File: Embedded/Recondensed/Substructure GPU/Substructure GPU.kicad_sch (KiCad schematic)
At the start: 37 parts, among them J1 10171746-00021LF, J11 Substructure Power, J13 MicroSD, J2 HUB75 Right, J3 Display Power, J4 HUB75 Left, J5 Expansion Data, J6 Expansion PWR, SW2 RST, U2 74HC245D_653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

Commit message: Added LCSC Component IDs
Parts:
- removed BootSW1: SW_Push, Buttons:R-667843, symbol Switch:SW_Push
- removed SW2: RST, Buttons:R-667843, symbol Switch:SW_Push
- added S1: Boot, Buttons:SW_B3U-1000P, symbol Buttons:B3U-1000P
- added S2: RST, Buttons:SW_B3U-1000P, symbol Buttons:B3U-1000P
- C1, C10, C12, C2: LCSC (none) -> C1591
- C11, C8: LCSC (none) -> C84419
- C3, C4, C5: LCSC (none) -> C3039698
- C6: LCSC (none) -> C95843
- C7, C9: LCSC C95839 -> C3039698
- D1, D2: LCSC (none) -> C7207730
- D3: LCSC (none) -> C50603
- J1: footprint USBC:AMPHENOL_10171746-00021LF -> USBC:MOLEX_2171790001; LCSC (none) -> C3197684
- J13: LCSC (none) -> C587826
- J2, J4: LCSC C30734 -> C492425
- R1, R2: LCSC (none) -> C328432
- R4, R9: LCSC (none) -> C98220
- R7: value 155ohm min -> 147ohm; LCSC (none) -> C2930065
- R8: value 70ohm min -> 33ohm; LCSC (none) -> C105588
- U6: LCSC (none) -> C86781
- U7: LCSC (none) -> C134077
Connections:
- net GND: now also J1.A1B12 (GND_A), J1.B1A12 (GND_B), S1.2, S2.2; no longer J1.A1_B12 (GND_A), J1.B1_A12 (GND_B)
- net at C5.1, D3.A: now also J1.A4B9 (VBUS_A), J1.B4A9 (VBUS_B); no longer J1.A4_B9 (VBUS_A), J1.B4_A9 (VBUS_B)
- net at ESP1.27 (GPIO0/BOOT), R4.2: now also S1.1
- net at C6.2, ESP1.3 (EN), R9.2: now also S2.1

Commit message: Modified Tables per component to centralise LCSC IDs
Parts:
- ESP1, J11, J3, J5, J6, U5: now left out of the parts list
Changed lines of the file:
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@@
 		(unit 1)
 		(exclude_from_sim no)
-		(in_bom yes)
+		(in_bom no)
 		(on_board yes)
 		(dnp no)
@@
 			)
 		)
-		(property "PARTREV" "A"
+		(property "LCSC" "C3197684"
 			(at 31.75 38.1 0)
 			(effects
@@
 					(size 1.27 1.27)
 				)
-				(justify bottom)
 				(hide yes)
 			)
 		)
-		(property "STANDARD" "Manufacturer Recommendations"
+		(property "PARTREV" "A"
 			(at 31.75 38.1 0)
 			(effects
@@
 			)
 		)
-		(property "MAXIMUM_PACKAGE_HEIGHT" "3.16 mm"
+		(property "STANDARD" "Manufacturer Recommendations"
 			(at 31.75 38.1 0)
 			(effects
@@
 			)
 		)
-		(property "MANUFACTURER" "Amphenol"
+		(property "MAXIMUM_PACKAGE_HEIGHT" "3.16 mm"
 			(at 31.75 38.1 0)
 			(effects
@@
 			)
 		)
-		(property "LCSC" "C3197684"
+		(property "MANUFACTURER" "Amphenol"
 			(at 31.75 38.1 0)
 			(effects
@@
 					(size 1.27 1.27)
 				)
+				(justify bottom)
 				(hide yes)
 			)
@@
 		(unit 1)
 		(exclude_from_sim no)
-		(in_bom yes)
+		(in_bom no)
 		(on_board yes)
 		(dnp no)
@@
 			)
 		)
+		(property "LCSC" "C5625"
+			(at 280.67 213.36 0)
+			(effects
+				(font
+					(size 1.27 1.27)
+				)
+				(hide yes)
+			)
+		)
 		(property "MF" "Nexperia USA"
 			(at 280.67 213.36 0)
@@
 			)
 		)
-		(property "LCSC" "C5625"
-			(at 280.67 213.36 0)
-			(effects
-				(font
-					(size 1.27 1.27)
-				)
-				(hide yes)
-			)
-		)
 		(pin "20"
 		)
@@
 			)
 		)
+		(property "LCSC" "C5625"
+			(at 356.87 213.36 0)
+			(effects
+				(font
+					(size 1.27 1.27)
+				)
+				(hide yes)
+			)
+		)
 		(property "MF" "Nexperia USA"
 			(at 356.87 213.36 0)
@@
 			)
 		)
-		(property "LCSC" "C5625"
-			(at 356.87 213.36 0)
-			(effects
-				(font
-					(size 1.27 1.27)
-				)
-				(hide yes)
-			)
-		)
 		(pin "20"
 		)
@@
 		(unit 1)
 		(exclude_from_sim no)
-		(in_bom yes)
+		(in_bom no)
 		(on_board yes)
 		(dnp no)
@@
 			)
 		)
+		(property "LCSC" "C231329"
+			(at 250.19 55.88 90)
+			(effects
+				(font
+					(size 1.27 1.27)
+				)
+				(hide yes)
+			)
+		)
 		(property "MF" "Omron"
 			(at 250.19 55.88 0)
@@
 			)
 		)
-		(property "LCSC" "C231329"
-			(at 250.19 55.88 90)
-			(effects
-				(font
-					(size 1.27 1.27)
-				)
-				(hide yes)
-			)
-		)
 		(pin "2"
 		)
@@
 			)
 		)
+		(property "LCSC" "C231329"
+			(at 393.7 71.12 90)
+			(effects
+				(font
+					(size 1.27 1.27)
+				)
+				(hide yes)
+			)
+		)
 		(property "MF" "Omron"
 			(at 393.7 71.12 0)
@@
 			)
 		)
-		(property "LCSC" "C231329"
-			(at 393.7 71.12 90)
-			(effects
-				(font
-					(size 1.27 1.27)
-				)
-				(hide yes)
-			)
-		)
 		(pin "2"
 		)
@@
 		(unit 1)
 		(exclude_from_sim no)
-		(in_bom yes)
+		(in_bom no)
 		(on_board yes)
 		(dnp no)
@@
 		(unit 1)
 		(exclude_from_sim no)
-		(in_bom yes)
+		(in_bom no)
 		(on_board yes)
 		(dnp no)
@@
 		(unit 1)
 		(exclude_from_sim no)
-		(in_bom yes)
+		(in_bom no)
 		(on_board yes)
 		(dnp no)
@@
 			)
 		)
-		(property "MF" "Nexperia USA Inc."
+		(property "LCSC" "C50603"
 			(at 82.55 26.67 0)
 			(effects
@@
 					(size 1.27 1.27)
 				)
-				(justify bottom)
 				(hide yes)
 			)
 		)
-		(property "DESCRIPTION" "Diode Schottky 30 V 5A Surface Mount SOD-128/CFP5"
+		(property "MF" "Nexperia USA Inc."
 			(at 82.55 26.67 0)
 			(effects
@@
 			)
 		)
-		(property "PACKAGE" "SOD-128 Nexperia USA Inc."
+		(property "DESCRIPTION" "Diode Schottky 30 V 5A Surface Mount SOD-128/CFP5"
 			(at 82.55 26.67 0)
 			(effects
@@
 			)
 		)
-		(property "PRICE" "None"
+		(property "PACKAGE" "SOD-128 Nexperia USA Inc."
 			(at 82.55 26.67 0)
 			(effects
@@
 			)
 		)
-		(property "MP" "PMEG3050EP,115"
+		(property "PRICE" "None"
 			(at 82.55 26.67 0)
 			(effects
@@
 			)
 		)
-		(property "AVAILABILITY" "In Stock"
+		(property "MP" "PMEG3050EP,115"
 			(at 82.55 26.67 0)
 			(effects
@@
 			)
 		)
-		(property "PURCHASE-URL" "https://pricing.snapeda.com/search/part/PMEG3050EP,115/?ref=eda"
+		(property "AVAILABILITY" "In Stock"
 			(at 82.55 26.67 0)
 			(effects
@@
 			)
 		)
-		(property "LCSC" "C50603"
+		(property "PURCHASE-URL" "https://pricing.snapeda.com/search/part/PMEG3050EP,115/?ref=eda"
 			(at 82.55 26.67 0)
 			(effects
@@
 					(size 1.27 1.27)
 				)
+				(justify bottom)
 				(hide yes)
 			)

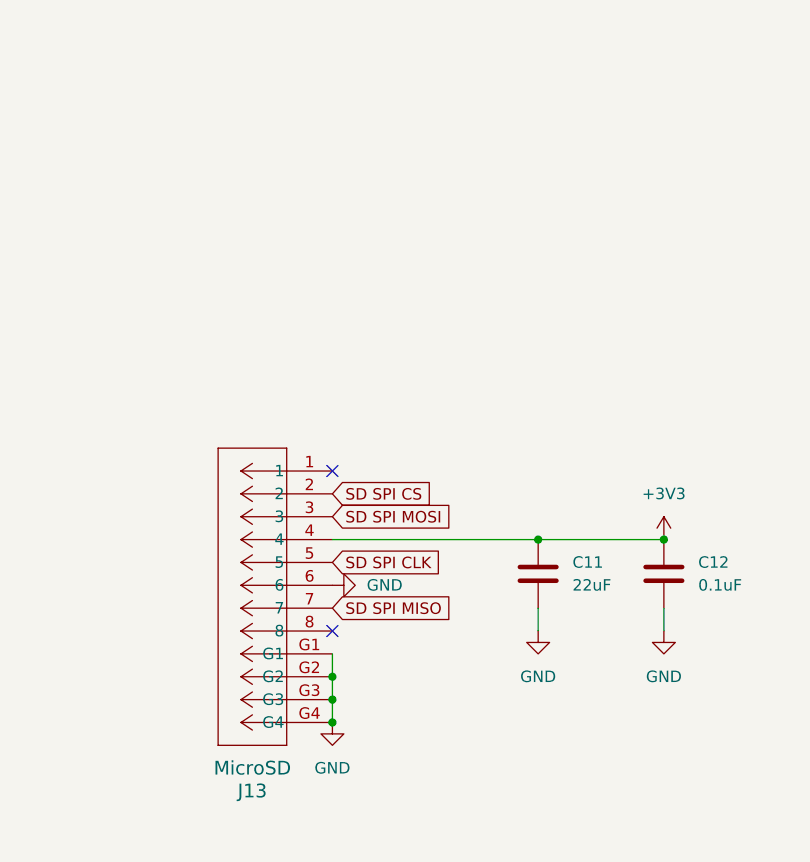
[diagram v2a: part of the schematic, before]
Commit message: Added Pullups for MicroSD & Modified Silkscreen
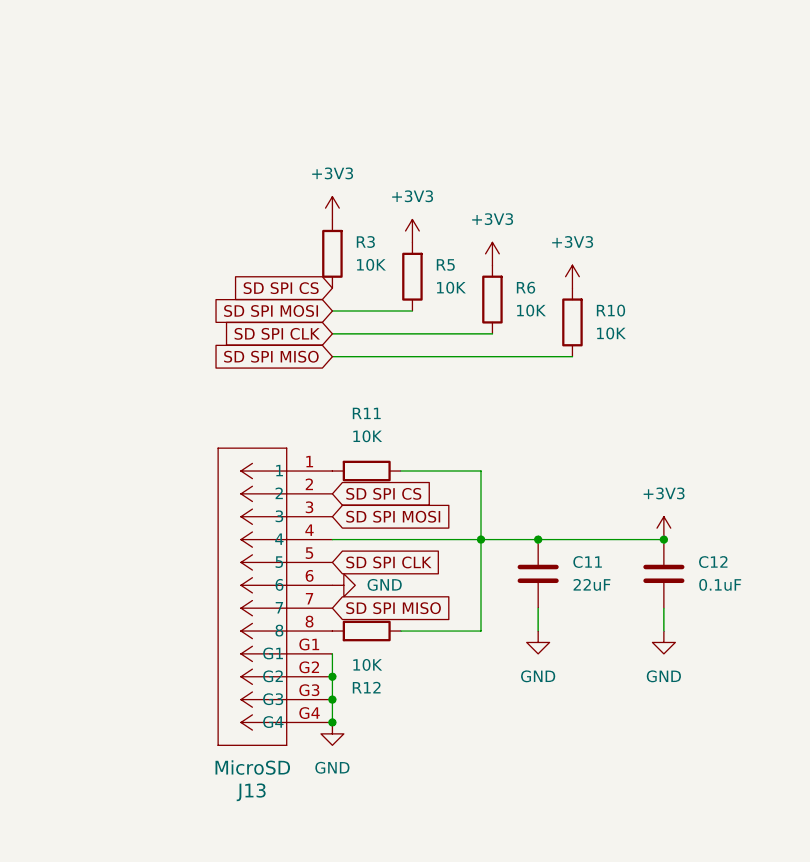
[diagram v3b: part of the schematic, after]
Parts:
- added R10, R11, R12, R3, R5, R6: 10K, Resistor_SMD:R_0603_1608Metric, symbol Device:R
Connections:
- net +3V3: now also R10.2, R11.1, R12.1, R3.2, R5.2, R6.2
- net SD SPI CLK: now also R6.1
- net SD SPI CS: now also R3.1
- net SD SPI MISO: now also R10.1
- net SD SPI MOSI: now also R5.1
- net at J13.1: now also R11.2
- net at J13.8: now also R12.2
- no-connect marks 11 -> 9
